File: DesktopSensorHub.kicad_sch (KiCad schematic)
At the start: 18 parts, among them J1 USB_C_Receptacle_USB2.0, SW1 SW_Push, U1 RP2040, U2 APDS-9960, U3 AP2112K-3.3, U4 W25Q16JVSS

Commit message: rev1 schematic finished
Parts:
- removed U4: W25Q16JVSS, Package_SO:SOIC-8_5.23x5.23mm_P1.27mm, symbol W25Q16JVSS:W25Q16JVSS
- added C10, C9: 27p, symbol Device:C
- added C11, C21: 1u, symbol Device:C
- added C12, C13, C14, C15, C16, C17, C18, C19, C20, C8: 100n, symbol Device:C
- added C6, C7: 10u, symbol Device:C
- added D1: ESD9B3.3ST5G, Diode_SMD:D_SOD-923, symbol Diode:ESD9B3.3ST5G
- added R6, R8, R9: 10K, symbol Device:R
- added R7: 1K, symbol Device:R
- added TP1, TP2, TP3: TestPoint, symbol Connector:TestPoint
- added U5: W25Q32JVSS, Package_SO:SOIC-8_5.23x5.23mm_P1.27mm, symbol Memory_Flash:W25Q32JVSS
- added Y1: 12MHZ, Crystal:Crystal_SMD_HC49-SD, symbol Device:Crystal
- C1, C2: value 47pF -> 47p
- C3, C4: value 1uF -> 1u
- C5: value 100uF -> 100u
- R5: value 10k -> 10K
- RUSB1, RUSB2: value 5.1k -> 5.1K
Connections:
- net +3V3: now also C7.1, C8.1, R6.1, R8.1, R9.1, U5.8 (VCC)
- net GND: now also U1.19 (TESTEN), U1.57 (GND), C10.1, C11.2, C12.2, C13.2, C14.2, C15.2, C16.2, C17.2, C18.2, C19.2, C20.2, C21.2, C6.2, C7.2, C8.2, C9.1, D1.2 (A2), TP2.1, U5.4 (GND)
- net +3.3V: now reaches U1.1 (IOVDD), U1.10 (IOVDD), U1.22 (IOVDD), U1.33 (IOVDD), U1.42 (IOVDD), U1.49 (IOVDD)
- net +3.3V: now also U1.43 (ADC_AVDD), U1.44 (VREG_IN), U1.48 (USB_VDD), C14.1, C15.1, C16.1, C17.1, C18.1, C19.1, C20.1, C21.1
- net at U1.20 (XIN): now also C9.2, Y1.1
- net at U1.21 (XOUT): now also R7.2
- net +1V1: now reaches U1.23 (DVDD), U1.50 (DVDD)
- net +1V1: now also U1.45 (VREG_VOUT), C11.1, C12.1, C13.1
- net at U1.26 (RUN): now also R6.2, TP1.1
- net at U1.27 (GPIO16): now also U2.7 (SCL), R9.2
- net at U1.28 (GPIO17): now also U2.1 (SDA), R8.2
- net at U1.29 (GPIO18): now also R5.2, U2.2 (INT)
- net at U1.51 (QSPI_SD3): now also U5.7 (IO3)
- net at U1.52 (QSPI_SCLK): now also U5.6 (CLK)
- net at U1.53 (QSPI_SD0): now also U5.5 (DI(IO0))
- net at U1.54 (QSPI_SD2): now also U5.3 (IO2)
- net at U1.55 (QSPI_SD1): now also U5.2 (DO(IO1))
- net at R1.1, U1.56 (QSPI_SS): now also U5.1 (~{CS})
- net at J1.A4 (VBUS), J1.A9 (VBUS), J1.B4 (VBUS)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: now also C6.1
- net at R1.2, SW1.2: now also D1.1 (A1), TP3.1
- new net: C10.2, R7.1, Y1.2
- no-connect marks 0 -> 31
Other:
- moved on the sheet: C1, C2, C3, C4, C5, J1, R1, R2, R3, R4, R5, RUSB1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

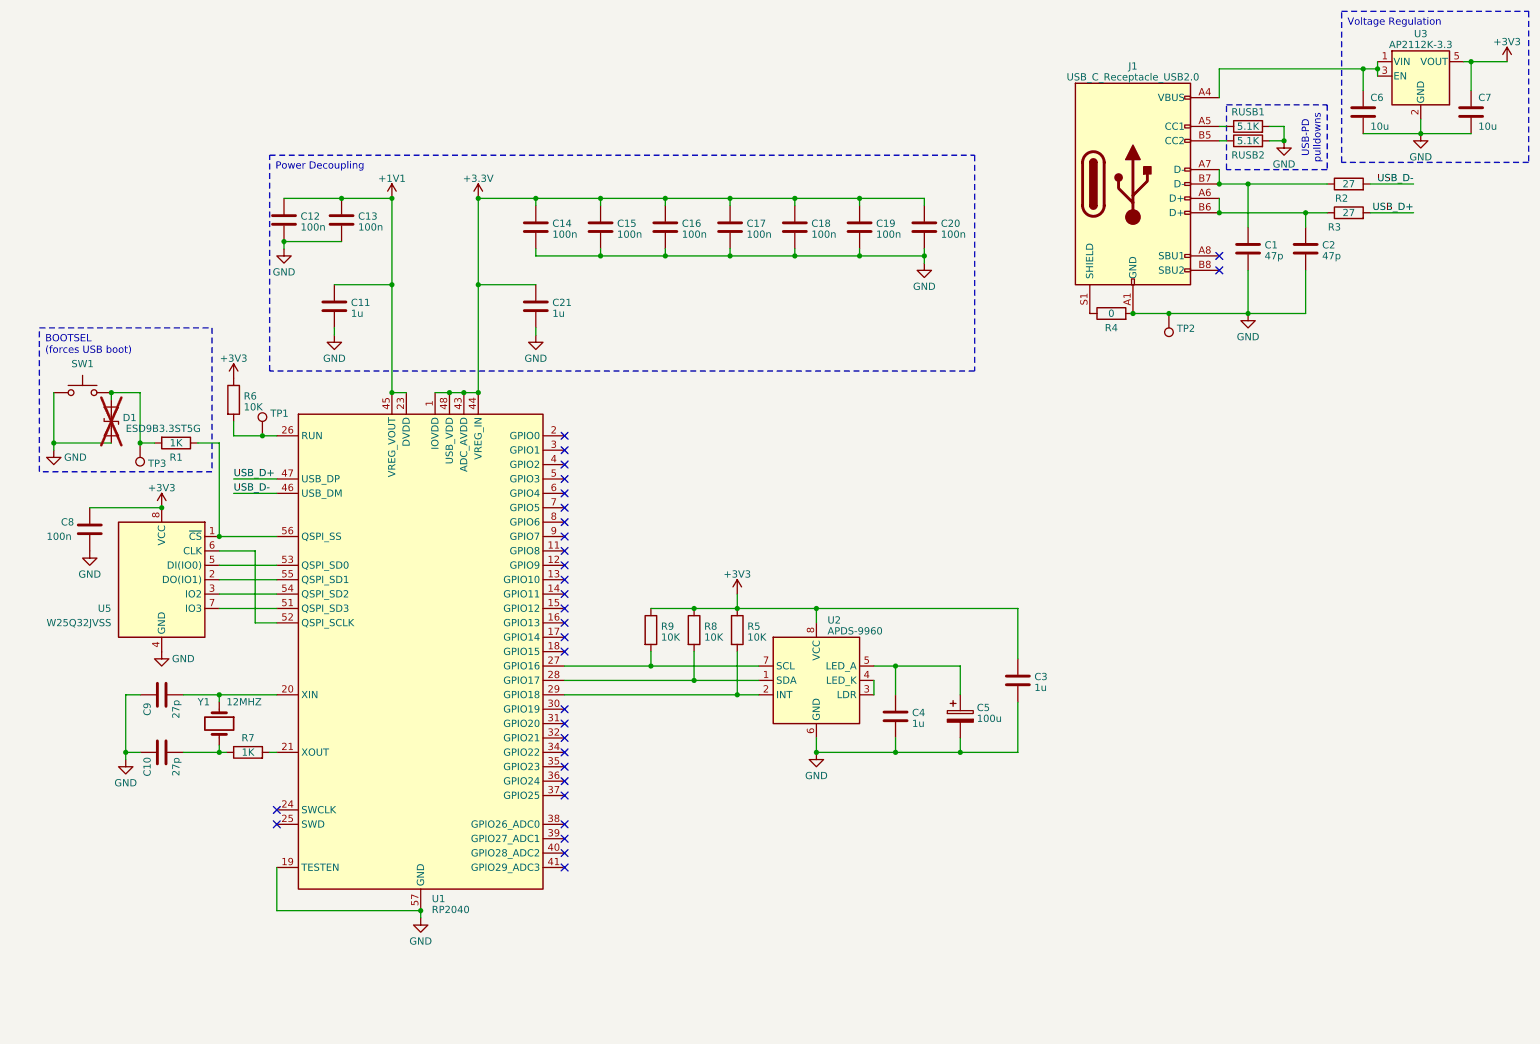
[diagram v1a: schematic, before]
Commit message: mark additional components as do not populate
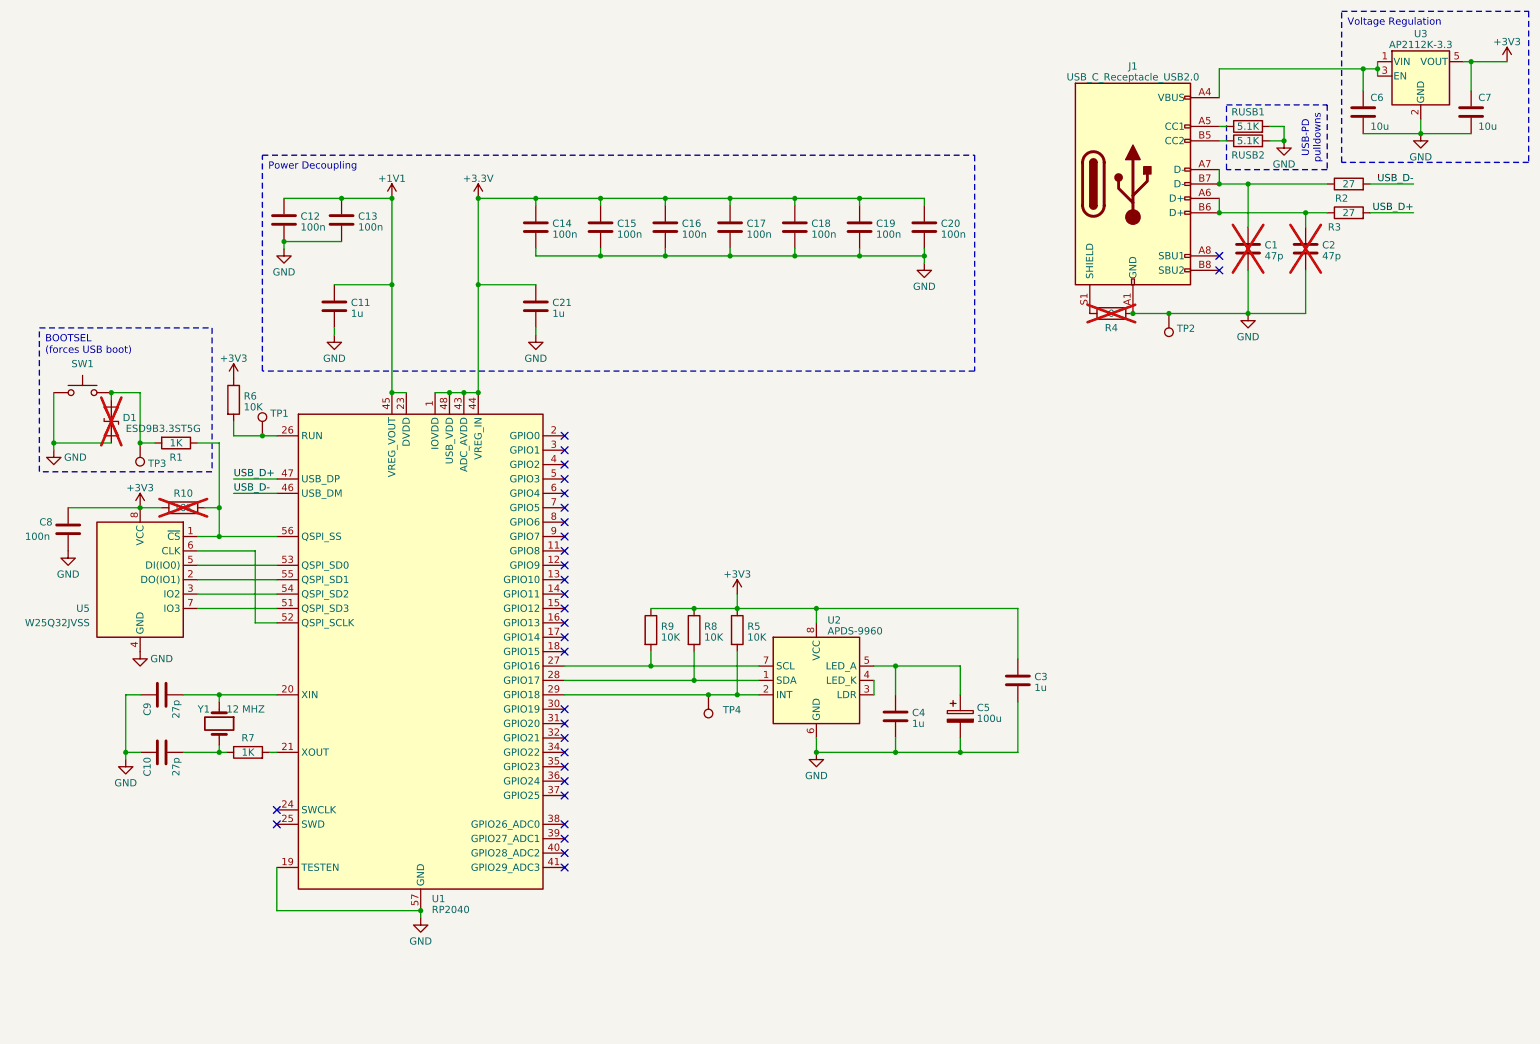
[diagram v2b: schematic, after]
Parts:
- added R10: 10K, Resistor_SMD:R_0805_2012Metric, symbol Device:R
- added TP4: TestPoint, TestPoint:TestPoint_Pad_D2.0mm, symbol Connector:TestPoint
- C1, C2: footprint (none) -> Capacitor_SMD:C_0603_1608Metric; now not fitted
- C10, C9: footprint (none) -> Capacitor_SMD:C_1206_3216Metric
- C12, C13, C14, C15, C16, C17, C18, C19, C20, C8: footprint (none) -> Capacitor_SMD:C_0201_0603Metric
- J1: footprint (none) -> Connector_USB:USB_C_Receptacle_Molex_105450-0101
- R1, R2, R3, R7, RUSB1, RUSB2: footprint (none) -> Resistor_SMD:R_0402_1005Metric
- R4: footprint (none) -> Resistor_SMD:R_0805_2012Metric_Pad1.20x1.40mm_HandSolder; now not fitted; now left out of the parts list
- R5, R6, R8, R9: footprint (none) -> Resistor_SMD:R_0805_2012Metric
- SW1: value SW_Push -> TS02-66-50-BK-160-LCR-D; footprint (none) -> Button_Switch_THT:SW_PUSH_6mm_H5mm
- TP1, TP2, TP3: footprint (none) -> TestPoint:TestPoint_Pad_D2.0mm
- Y1: value 12MHZ -> 12 MHZ; MPN (none) -> ABLS-12.000MHZ-B4-T
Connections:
- net +3V3: now also R10.1
- net at R5.2, U1.29 (GPIO18), U2.2 (INT): now also TP4.1
- net at R1.1, U1.56 (QSPI_SS), U5.1 (~{CS}): now also R10.2
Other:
- moved on the sheet: C8, U5

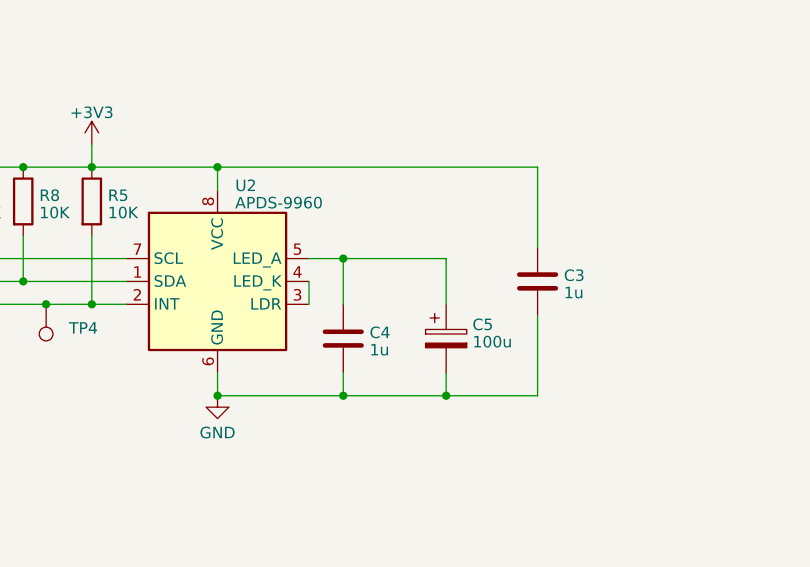
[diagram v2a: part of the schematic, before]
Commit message: remove 100uF capacitor since LED not exposed to be driven externally anyways
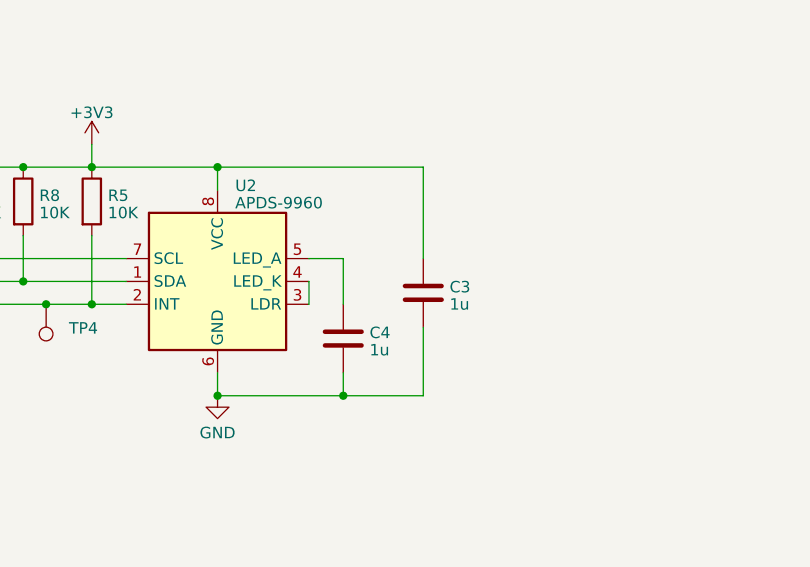
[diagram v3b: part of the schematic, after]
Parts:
- removed C5: 100u, symbol Device:C_Polarized
- C6, C7: footprint (none) -> Capacitor_SMD:C_0201_0603Metric
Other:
- moved on the sheet: C3
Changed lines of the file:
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@@
   (junction (at 83.82 175.26) (diameter 0) (color 0 0 0 0)
   )
-  (junction (at 179.07 147.32) (diameter 0) (color 0 0 0 0)
-  )
   (junction (at 93.98 64.77) (diameter 0) (color 0 0 0 0)
   )
   (junction (at 240.03 52.07) (diameter 0) (color 0 0 0 0)
-  )
-  (junction (at 167.64 132.08) (diameter 0) (color 0 0 0 0)
   )
   (junction (at 104.14 49.53) (diameter 0) (color 0 0 0 0)
@@
     (stroke (width 0) (type default))
   )
-  (wire (pts (xy 189.23 147.32) (xy 189.23 138.43))
+  (wire (pts (xy 176.53 147.32) (xy 176.53 139.7))
     (stroke (width 0) (type default))
   )
@@
     (stroke (width 0) (type default))
   )
-  (wire (pts (xy 189.23 121.92) (xy 189.23 130.81))
+  (wire (pts (xy 176.53 121.92) (xy 176.53 132.08))
     (stroke (width 0) (type default))
   )
@@
     (stroke (width 0) (type default))
   )
-  (wire (pts (xy 153.67 121.92) (xy 189.23 121.92))
+  (wire (pts (xy 153.67 121.92) (xy 176.53 121.92))
     (stroke (width 0) (type default))
   )
@@
     (stroke (width 0) (type default))
   )
-  (wire (pts (xy 179.07 144.78) (xy 179.07 147.32))
-    (stroke (width 0) (type default))
-  )
   (wire (pts (xy 41.91 137.16) (xy 48.26 137.16))
     (stroke (width 0) (type default))
@@
     (stroke (width 0) (type default))
   )
-  (wire (pts (xy 167.64 147.32) (xy 179.07 147.32))
+  (wire (pts (xy 167.64 147.32) (xy 176.53 147.32))
     (stroke (width 0) (type default))
   )
@@
     (stroke (width 0) (type default))
   )
-  (wire (pts (xy 179.07 137.16) (xy 179.07 132.08))
-    (stroke (width 0) (type default))
-  )
   (wire (pts (xy 59.69 58.42) (xy 59.69 57.15))
     (stroke (width 0) (type default))
@@
     (stroke (width 0) (type default))
   )
-  (wire (pts (xy 179.07 147.32) (xy 189.23 147.32))
-    (stroke (width 0) (type default))
-  )
   (wire (pts (xy 251.46 52.07) (xy 259.08 52.07))
     (stroke (width 0) (type default))
@@
   )
   (wire (pts (xy 250.19 26.67) (xy 250.19 30.48))
-    (stroke (width 0) (type default))
-  )
-  (wire (pts (xy 179.07 132.08) (xy 167.64 132.08))
     (stroke (width 0) (type default))
   )
@@
       (effects (font (size 1.27 1.27)) (justify left))
     )
-    (property "Footprint" "" (at 251.1552 38.1 0)
+    (property "Footprint" "Capacitor_SMD:C_0201_0603Metric" (at 251.1552 38.1 0)
       (effects (font (size 1.27 1.27)) hide)
     )
@@
       (effects (font (size 1.27 1.27)) (justify left))
     )
-    (property "Footprint" "" (at 270.2052 38.1 0)
+    (property "Footprint" "Capacitor_SMD:C_0201_0603Metric" (at 270.2052 38.1 0)
       (effects (font (size 1.27 1.27)) hide)
     )
@@
     )
   )
-  (symbol (lib_id "Device:C") (at 189.23 134.62 0) (unit 1)
-    (in_bom yes) (on_board yes) (dnp no) (fields_autoplaced)
-    (property "Reference" "C3" (at 192.151 133.9763 0)
-      (effects (font (size 1.27 1.27)) (justify left))
-    )
-    (property "Value" "1u" (at 192.151 135.8973 0)
-      (effects (font (size 1.27 1.27)) (justify left))
-    )
-    (property "Footprint" "" (at 190.1952 138.43 0)
-      (effects (font (size 1.27 1.27)) hide)
-    )
-    (property "Datasheet" "~" (at 189.23 134.62 0)
+  (symbol (lib_id "Device:C") (at 176.53 135.89 0) (unit 1)
+    (in_bom yes) (on_board yes) (dnp no) (fields_autoplaced)
+    (property "Reference" "C3" (at 179.451 135.2463 0)
+      (effects (font (size 1.27 1.27)) (justify left))
+    )
+    (property "Value" "1u" (at 179.451 137.1673 0)
+      (effects (font (size 1.27 1.27)) (justify left))
+    )
+    (property "Footprint" "" (at 177.4952 139.7 0)
+      (effects (font (size 1.27 1.27)) hide)
+    )
+    (property "Datasheet" "~" (at 176.53 135.89 0)
       (effects (font (size 1.27 1.27)) hide)
     )
@@
         )
       )
-    )
-  )
-  (symbol (lib_id "Device:C_Polarized") (at 179.07 140.97 0) (unit 1)
-    (in_bom yes) (on_board yes) (dnp no) (fields_autoplaced)
-    (property "Reference" "C5" (at 181.991 139.4373 0)
-      (effects (font (size 1.27 1.27)) (justify left))
-    )
-    (property "Value" "100u" (at 181.991 141.3583 0)
-      (effects (font (size 1.27 1.27)) (justify left))
-    )
-    (property "Footprint" "" (at 180.0352 144.78 0)
-      (effects (font (size 1.27 1.27)) hide)
-    )
-    (property "Datasheet" "~" (at 179.07 140.97 0)
-      (effects (font (size 1.27 1.27)) hide)
-    )
-    (pin "1")
-    (pin "2")
-    (instances
-      (project "DesktopSensorHub"
-        (path "/48c0c7ef-0fb2-4c47-a984-821bb99e66ea"
-          (reference "C5") (unit 1)
-        )
-      )

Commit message: add missing footprint for 1uF capacitors
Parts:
- C11, C21, C3, C4: footprint (none) -> Capacitor_SMD:C_0603_1608Metric
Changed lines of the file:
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@@
       (effects (font (size 1.27 1.27)) (justify left))
     )
-    (property "Footprint" "" (at 168.6052 144.78 0)
+    (property "Footprint" "Capacitor_SMD:C_0603_1608Metric" (at 168.6052 144.78 0)
       (effects (font (size 1.27 1.27)) hide)
     )
@@
       (effects (font (size 1.27 1.27)) (justify left))
     )
-    (property "Footprint" "" (at 177.4952 139.7 0)
+    (property "Footprint" "Capacitor_SMD:C_0603_1608Metric" (at 177.4952 139.7 0)
       (effects (font (size 1.27 1.27)) hide)
     )
@@
       (effects (font (size 1.27 1.27)) (justify left))
     )
-    (property "Footprint" "" (at 69.5452 72.39 0)
+    (property "Footprint" "Capacitor_SMD:C_0603_1608Metric" (at 69.5452 72.39 0)
       (effects (font (size 1.27 1.27)) hide)
     )
@@
       (effects (font (size 1.27 1.27)) (justify left))
     )
-    (property "Footprint" "" (at 105.1052 72.39 0)
-      (effects (font (size 1.27 1.27)) hide)
-    )
+    (property "Footprint" "Capacitor_SMD:C_0603_1608Metric" (at 105.1052 72.39 0)
+      (effects (font (size 1.27 1.27)) hide)
+    )
